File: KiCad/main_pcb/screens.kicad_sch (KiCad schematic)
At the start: 21 parts, among them J3 Conn_01x13, J4 Conn_01x07, J5 Conn_01x07, U2 TXB0104D, U3 TXB0104D, U4 TXB0104D

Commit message: chore(migration): Migrates to homebrew symbols for PCB.
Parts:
- U1: renamed from U4; footprint Package_SO:SOIC-14_3.9x8.7mm_P1.27mm -> Lilibrary:SOIC-14_TXB0104DR
- U2, U3: footprint Package_SO:SOIC-14_3.9x8.7mm_P1.27mm -> Lilibrary:SOIC-14_TXB0104DR
- renumbered C10 to C1, C8 to C10, C12 to C2, C11 to C3, C5 to C4, C6 to C5, C13 to C6, C9 to C8, C7 to C9, J4 to J1, J5 to J2, R6 to R1
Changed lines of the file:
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@@
 		(dnp no)
 		(fields_autoplaced yes)
-		(property "Reference" "C5"
+		(property "Reference" "C4"
 			(at 54.61 107.9499 0)
 			(effects
@@
 			(project "main_pcb"
 				(path "/ecf3cf27-e370-4cc5-86a4-628206277f58/b75c720d-c507-4908-ace0-f9d76db017d1"
-					(reference "C5")
+					(reference "C4")
 					(unit 1)
 				)
@@
 		(dnp no)
 		(fields_autoplaced yes)
-		(property "Reference" "C9"
+		(property "Reference" "C8"
 			(at 130.81 68.58 90)
 			(effects
@@
 			(project "main_pcb"
 				(path "/ecf3cf27-e370-4cc5-86a4-628206277f58/b75c720d-c507-4908-ace0-f9d76db017d1"
-					(reference "C9")
+					(reference "C8")
 					(unit 1)
 				)
@@
 		(dnp no)
 		(fields_autoplaced yes)
-		(property "Reference" "U4"
+		(property "Reference" "U1"
 			(at 240.03 110.4198 90)
 			(effects
@@
 			)
 		)
-		(property "Footprint" "Package_SO:SOIC-14_3.9x8.7mm_P1.27mm"
+		(property "Footprint" "Lilibrary:SOIC-14_TXB0104DR"
 			(at 237.49 116.84 0)
 			(effects
@@
 			(project "main_pcb"
 				(path "/ecf3cf27-e370-4cc5-86a4-628206277f58/b75c720d-c507-4908-ace0-f9d76db017d1"
-					(reference "U4")
+					(reference "U1")
 					(unit 1)
 				)
@@
 		(dnp no)
 		(fields_autoplaced yes)
-		(property "Reference" "R6"
+		(property "Reference" "R1"
 			(at 165.1 97.79 90)
 			(effects
@@
 			(project "main_pcb"
 				(path "/ecf3cf27-e370-4cc5-86a4-628206277f58/b75c720d-c507-4908-ace0-f9d76db017d1"
-					(reference "R6")
+					(reference "R1")
 					(unit 1)
 				)
@@
 		(dnp no)
 		(fields_autoplaced yes)
-		(property "Reference" "C11"
+		(property "Reference" "C3"
 			(at 186.69 107.9499 0)
 			(effects
@@
 			(project "main_pcb"
 				(path "/ecf3cf27-e370-4cc5-86a4-628206277f58/b75c720d-c507-4908-ace0-f9d76db017d1"
-					(reference "C11")
+					(reference "C3")
 					(unit 1)
 				)
@@
 		(dnp no)
 		(fields_autoplaced yes)
-		(property "Reference" "C7"
+		(property "Reference" "C9"
 			(at 116.84 107.9499 0)
 			(effects
@@
 			(project "main_pcb"
 				(path "/ecf3cf27-e370-4cc5-86a4-628206277f58/b75c720d-c507-4908-ace0-f9d76db017d1"
-					(reference "C7")
+					(reference "C9")
 					(unit 1)
 				)
@@
 		(dnp no)
 		(fields_autoplaced yes)
-		(property "Reference" "C6"
+		(property "Reference" "C5"
 			(at 62.23 123.1899 0)
 			(effects
@@
 			(project "main_pcb"
 				(path "/ecf3cf27-e370-4cc5-86a4-628206277f58/b75c720d-c507-4908-ace0-f9d76db017d1"
-					(reference "C6")
+					(reference "C5")
 					(unit 1)
 				)
@@
 		(dnp no)
 		(fields_autoplaced yes)
-		(property "Reference" "J4"
+		(property "Reference" "J1"
 			(at 189.23 46.99 90)
 			(effects
@@
 			(project "main_pcb"
 				(path "/ecf3cf27-e370-4cc5-86a4-628206277f58/b75c720d-c507-4908-ace0-f9d76db017d1"
-					(reference "J4")
+					(reference "J1")
 					(unit 1)
 				)
@@
 		(dnp no)
 		(fields_autoplaced yes)
-		(property "Reference" "C10"
+		(property "Reference" "C1"
 			(at 176.53 68.58 90)
 			(effects
@@
 			(project "main_pcb"
 				(path "/ecf3cf27-e370-4cc5-86a4-628206277f58/b75c720d-c507-4908-ace0-f9d76db017d1"
-					(reference "C10")
+					(reference "C1")
 					(unit 1)
 				)
@@
 		(dnp no)
 		(fields_autoplaced yes)
-		(property "Reference" "J5"
+		(property "Reference" "J2"
 			(at 222.25 46.99 90)
 			(effects
@@
 			(project "main_pcb"
 				(path "/ecf3cf27-e370-4cc5-86a4-628206277f58/b75c720d-c507-4908-ace0-f9d76db017d1"
-					(reference "J5")
+					(reference "J2")
 					(unit 1)
 				)
@@
 			)
 		)
-		(property "Footprint" "Package_SO:SOIC-14_3.9x8.7mm_P1.27mm"
+		(property "Footprint" "Lilibrary:SOIC-14_TXB0104DR"
 			(at 105.41 116.84 0)
 			(effects
@@
 		(dnp no)
 		(fields_autoplaced yes)
-		(property "Reference" "C12"
+		(property "Reference" "C2"
 			(at 194.31 123.1899 0)
 			(effects
@@
 			(project "main_pcb"
 				(path "/ecf3cf27-e370-4cc5-86a4-628206277f58/b75c720d-c507-4908-ace0-f9d76db017d1"
-					(reference "C12")
+					(reference "C2")
 					(unit 1)
 				)
@@
 		(dnp no)
 		(fields_autoplaced yes)
-		(property "Reference" "C8"
+		(property "Reference" "C10"
 			(at 124.46 123.1899 0)
 			(effects
@@
 			(project "main_pcb"
 				(path "/ecf3cf27-e370-4cc5-86a4-628206277f58/b75c720d-c507-4908-ace0-f9d76db017d1"
-					(reference "C8")
+					(reference "C10")
 					(unit 1)
 				)
@@
 		(dnp no)
 		(fields_autoplaced yes)
-		(property "Reference" "C13"
+		(property "Reference" "C6"
 			(at 209.55 55.88 90)
 			(effects
@@
 			(project "main_pcb"
 				(path "/ecf3cf27-e370-4cc5-86a4-628206277f58/b75c720d-c507-4908-ace0-f9d76db017d1"
-					(reference "C13")
+					(reference "C6")
 					(unit 1)
 				)
@@
 			)
 		)
-		(property "Footprint" "Package_SO:SOIC-14_3.9x8.7mm_P1.27mm"
+		(property "Footprint" "Lilibrary:SOIC-14_TXB0104DR"
 			(at 167.64 116.84 0)
 			(effects

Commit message: feat(pcb): I think that's about right
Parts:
- C1, C10, C2, C3, C4, C5, C6, C8, C9: footprint Capacitor_SMD:C_0603_1608Metric_Pad1.08x0.95mm_HandSolder -> Lilibrary:Capacitor_0603
- R1: footprint Resistor_SMD:R_0603_1608Metric_Pad0.98x0.95mm_HandSolder -> Lilibrary:Resistor_0603
- TP3, TP4, TP5, TP6, TP7: footprint TestPoint:TestPoint_Pad_D2.0mm -> Lilibrary:Test point
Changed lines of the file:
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@@
 			)
 		)
-		(property "Footprint" "Capacitor_SMD:C_0603_1608Metric_Pad1.08x0.95mm_HandSolder"
+		(property "Footprint" "Lilibrary:Capacitor_0603"
 			(at 59.3852 113.03 0)
 			(effects
@@
 			)
 		)
-		(property "Footprint" "Capacitor_SMD:C_0603_1608Metric_Pad1.08x0.95mm_HandSolder"
+		(property "Footprint" "Lilibrary:Capacitor_0603"
 			(at 134.62 62.5348 0)
 			(effects
@@
 			)
 		)
-		(property "Footprint" "Resistor_SMD:R_0603_1608Metric_Pad0.98x0.95mm_HandSolder"
+		(property "Footprint" "Lilibrary:Resistor_0603"
 			(at 165.1 95.758 90)
 			(effects
@@
 			)
 		)
-		(property "Footprint" "Capacitor_SMD:C_0603_1608Metric_Pad1.08x0.95mm_HandSolder"
+		(property "Footprint" "Lilibrary:Capacitor_0603"
 			(at 191.4652 113.03 0)
 			(effects
@@
 			)
 		)
-		(property "Footprint" "TestPoint:TestPoint_Pad_D2.0mm"
+		(property "Footprint" "Lilibrary:Test point"
 			(at 222.25 78.74 0)
 			(effects
@@
 			)
 		)
-		(property "Footprint" "Capacitor_SMD:C_0603_1608Metric_Pad1.08x0.95mm_HandSolder"
+		(property "Footprint" "Lilibrary:Capacitor_0603"
 			(at 121.6152 113.03 0)
 			(effects
@@
 			)
 		)
-		(property "Footprint" "Capacitor_SMD:C_0603_1608Metric_Pad1.08x0.95mm_HandSolder"
+		(property "Footprint" "Lilibrary:Capacitor_0603"
 			(at 57.4548 120.65 0)
 			(effects
@@
 			)
 		)
-		(property "Footprint" "Capacitor_SMD:C_0603_1608Metric_Pad1.08x0.95mm_HandSolder"
+		(property "Footprint" "Lilibrary:Capacitor_0603"
 			(at 180.34 62.5348 0)
 			(effects
@@
 			)
 		)
-		(property "Footprint" "TestPoint:TestPoint_Pad_D2.0mm"
+		(property "Footprint" "Lilibrary:Test point"
 			(at 93.98 97.79 0)
 			(effects
@@
 			)
 		)
-		(property "Footprint" "TestPoint:TestPoint_Pad_D2.0mm"
+		(property "Footprint" "Lilibrary:Test point"
 			(at 158.75 82.55 0)
 			(effects
@@
 			)
 		)
-		(property "Footprint" "Capacitor_SMD:C_0603_1608Metric_Pad1.08x0.95mm_HandSolder"
+		(property "Footprint" "Lilibrary:Capacitor_0603"
 			(at 189.5348 120.65 0)
 			(effects
@@
 			)
 		)
-		(property "Footprint" "Capacitor_SMD:C_0603_1608Metric_Pad1.08x0.95mm_HandSolder"
+		(property "Footprint" "Lilibrary:Capacitor_0603"
 			(at 119.6848 120.65 0)
 			(effects
@@
 			)
 		)
-		(property "Footprint" "Capacitor_SMD:C_0603_1608Metric_Pad1.08x0.95mm_HandSolder"
+		(property "Footprint" "Lilibrary:Capacitor_0603"
 			(at 213.36 62.5348 0)
 			(effects
@@
 			)
 		)
-		(property "Footprint" "TestPoint:TestPoint_Pad_D2.0mm"
+		(property "Footprint" "Lilibrary:Test point"
 			(at 194.31 83.82 0)
 			(effects
@@
 			)
 		)
-		(property "Footprint" "TestPoint:TestPoint_Pad_D2.0mm"
+		(property "Footprint" "Lilibrary:Test point"
 			(at 140.97 72.39 0)
 			(effects

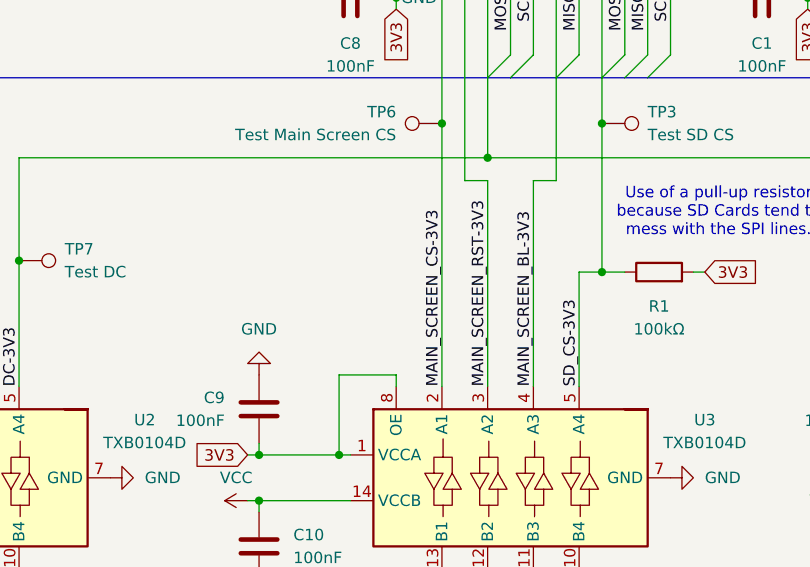
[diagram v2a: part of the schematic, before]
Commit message: feat(PCB): Adds two pins header for LED Backlight
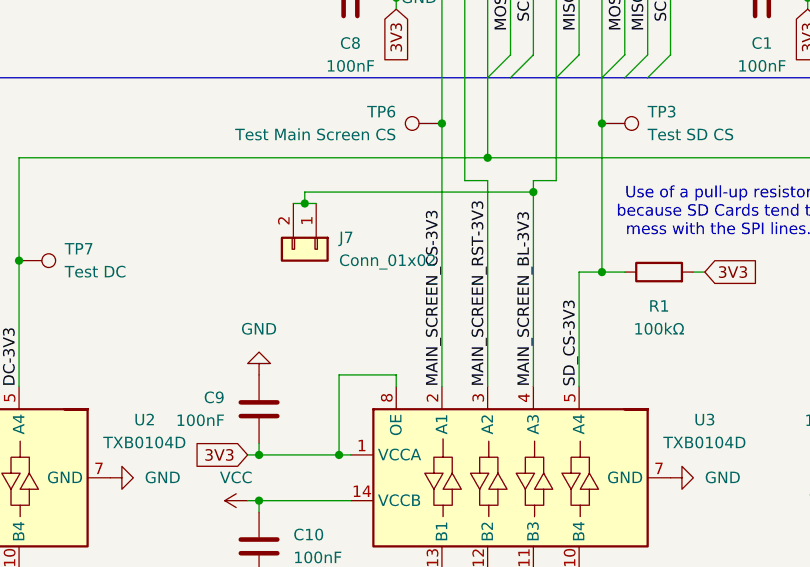
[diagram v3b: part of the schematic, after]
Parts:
- added J7: Conn_01x02, Connector_JST:JST_XH_B2B-XH-A_1x02_P2.50mm_Vertical, symbol Connector_Generic:Conn_01x02
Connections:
- net MAIN_SCREEN_BL-3V3: now also J7.1 (Pin_1), J7.2 (Pin_2)
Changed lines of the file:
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@@
 	)
 	(junction
+		(at 125.73 86.36)
+		(diameter 0)
+		(color 0 0 0 0)
+	)
+	(junction
 		(at 67.31 114.3)
 		(diameter 0)
@@
 	)
 	(junction
+		(at 151.13 85.09)
+		(diameter 0)
+		(color 0 0 0 0)
+	)
+	(junction
 		(at 158.75 77.47)
 		(diameter 0)
@@
 	(wire
 		(pts
-			(xy 146.05 83.82) (xy 143.51 83.82)
-		)
-		(stroke
-			(width 0)
-			(type default)
-		)
-	)
-	(wire
-		(pts
 			(xy 143.51 83.82) (xy 143.51 58.42)
 		)
@@
 	(wire
 		(pts
+			(xy 124.46 86.36) (xy 125.73 86.36)
+		)
+		(stroke
+			(width 0)
+			(type default)
+		)
+	)
+	(wire
+		(pts
 			(xy 156.21 93.98) (xy 158.75 93.98)
 		)
@@
 	(wire
 		(pts
+			(xy 125.73 86.36) (xy 127 86.36)
+		)
+		(stroke
+			(width 0)
+			(type default)
+		)
+	)
+	(wire
+		(pts
 			(xy 181.61 63.5) (xy 180.34 63.5)
 		)
@@
 	(wire
 		(pts
+			(xy 151.13 85.09) (xy 125.73 85.09)
+		)
+		(stroke
+			(width 0)
+			(type default)
+		)
+	)
+	(wire
+		(pts
 			(xy 214.63 58.42) (xy 214.63 63.5)
 		)
@@
 	(wire
 		(pts
+			(xy 143.51 83.82) (xy 146.05 83.82)
+		)
+		(stroke
+			(width 0)
+			(type default)
+		)
+	)
+	(wire
+		(pts
 			(xy 214.63 63.5) (xy 214.63 64.77)
 		)
@@
 		)
 	)
+	(wire
+		(pts
+			(xy 151.13 85.09) (xy 151.13 106.68)
+		)
+		(stroke
+			(width 0)
+			(type default)
+		)
+	)
 	(bus
 		(pts
@@
 	(wire
 		(pts
-			(xy 151.13 83.82) (xy 151.13 106.68)
+			(xy 151.13 83.82) (xy 151.13 85.09)
 		)
 		(stroke
@@
 	(wire
 		(pts
+			(xy 125.73 85.09) (xy 125.73 86.36)
+		)
+		(stroke
+			(width 0)
+			(type default)
+		)
+	)
+	(wire
+		(pts
 			(xy 146.05 83.82) (xy 146.05 106.68)
 		)
@@
 					(unit 1)
 				)
+			)
+		)
+	)
+	(symbol
+		(lib_id "Connector_Generic:Conn_01x02")
+		(at 127 91.44 270)
+		(unit 1)
+		(exclude_from_sim no)
+		(in_bom yes)
+		(on_board yes)
+		(dnp no)
+		(fields_autoplaced yes)
+		(property "Reference" "J7"
+			(at 129.54 90.1699 90)
+			(effects
+				(font
+					(size 1.27 1.27)
+				)
+				(justify left)
+			)
+		)
+		(property "Value" "Conn_01x02"
+			(at 129.54 92.7099 90)
+			(effects
+				(font
+					(size 1.27 1.27)
+				)
+				(justify left)
+			)
+		)
+		(property "Footprint" "Connector_JST:JST_XH_B2B-XH-A_1x02_P2.50mm_Vertical"
+			(at 127 91.44 0)
+			(effects
+				(font
+					(size 1.27 1.27)
+				)
+				(hide yes)
+			)
+		)
+		(property "Datasheet" "~"
+			(at 127 91.44 0)
+			(effects
+				(font
+					(size 1.27 1.27)
+				)
+				(hide yes)
+			)
+		)
+		(property "Description" "Generic connector, single row, 01x02, script generated (kicad-library-utils/schlib/autogen/connector/)"
+			(at 127 91.44 0)
+			(effects
+				(font
+					(size 1.27 1.27)
+				)
+				(hide yes)
+			)
+		)
+		(pin "2"
+		)
+		(pin "1"
+		)
+		(instances
+			(project "main_pcb"
+				(path "/ecf3cf27-e370-4cc5-86a4-628206277f58/b75c720d-c507-4908-ace0-f9d76db017d1"
+					(reference "J7")
+					(unit 1)
+				)

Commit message: feat(pcb): Adds all the remaning 3D models
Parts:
- J1, J2: footprint Connector_PinHeader_2.54mm:PinHeader_1x07_P2.54mm_Vertical -> Lilibrary:Pin_1x07_2.54mm_Vertical
- J3: footprint Connector_PinHeader_2.54mm:PinHeader_1x13_P2.54mm_Vertical -> Lilibrary:Pin_1x13_2.54mm_Vertical
- J7: footprint Connector_JST:JST_XH_B2B-XH-A_1x02_P2.50mm_Vertical -> Lilibrary:JST XH 2 pins
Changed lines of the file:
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@@
 			)
 		)
-		(property "Footprint" "Connector_PinHeader_2.54mm:PinHeader_1x07_P2.54mm_Vertical"
+		(property "Footprint" "Lilibrary:Pin_1x07_2.54mm_Vertical"
 			(at 189.23 53.34 0)
 			(effects
@@
 			)
 		)
-		(property "Footprint" "Connector_PinHeader_2.54mm:PinHeader_1x07_P2.54mm_Vertical"
+		(property "Footprint" "Lilibrary:Pin_1x07_2.54mm_Vertical"
 			(at 222.25 53.34 0)
 			(effects
@@
 			)
 		)
-		(property "Footprint" "Connector_PinHeader_2.54mm:PinHeader_1x13_P2.54mm_Vertical"
+		(property "Footprint" "Lilibrary:Pin_1x13_2.54mm_Vertical"
 			(at 151.13 53.34 0)
 			(effects
@@
 			)
 		)
-		(property "Footprint" "Connector_JST:JST_XH_B2B-XH-A_1x02_P2.50mm_Vertical"
+		(property "Footprint" "Lilibrary:JST XH 2 pins"
 			(at 127 91.44 0)
 			(effects

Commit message: chore: Adds 3D models to footprint, instead of adding manually when placing components :3
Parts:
- U1, U2, U3: footprint Lilibrary:SOIC-14_TXB0104DR -> Package_SO:SOIC-14_3.9x8.7mm_P1.27mm
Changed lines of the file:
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@@
 			)
 		)
-		(property "Footprint" "Lilibrary:SOIC-14_TXB0104DR"
+		(property "Footprint" "Package_SO:SOIC-14_3.9x8.7mm_P1.27mm"
 			(at 237.49 116.84 0)
 			(effects
@@
 			)
 		)
-		(property "Footprint" "Lilibrary:SOIC-14_TXB0104DR"
+		(property "Footprint" "Package_SO:SOIC-14_3.9x8.7mm_P1.27mm"
 			(at 105.41 116.84 0)
 			(effects
@@
 			)
 		)
-		(property "Footprint" "Lilibrary:SOIC-14_TXB0104DR"
+		(property "Footprint" "Package_SO:SOIC-14_3.9x8.7mm_P1.27mm"
 			(at 167.64 116.84 0)
 			(effects
